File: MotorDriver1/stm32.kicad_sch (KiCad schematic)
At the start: 1 part, among them IC1 STM32C092RCT6

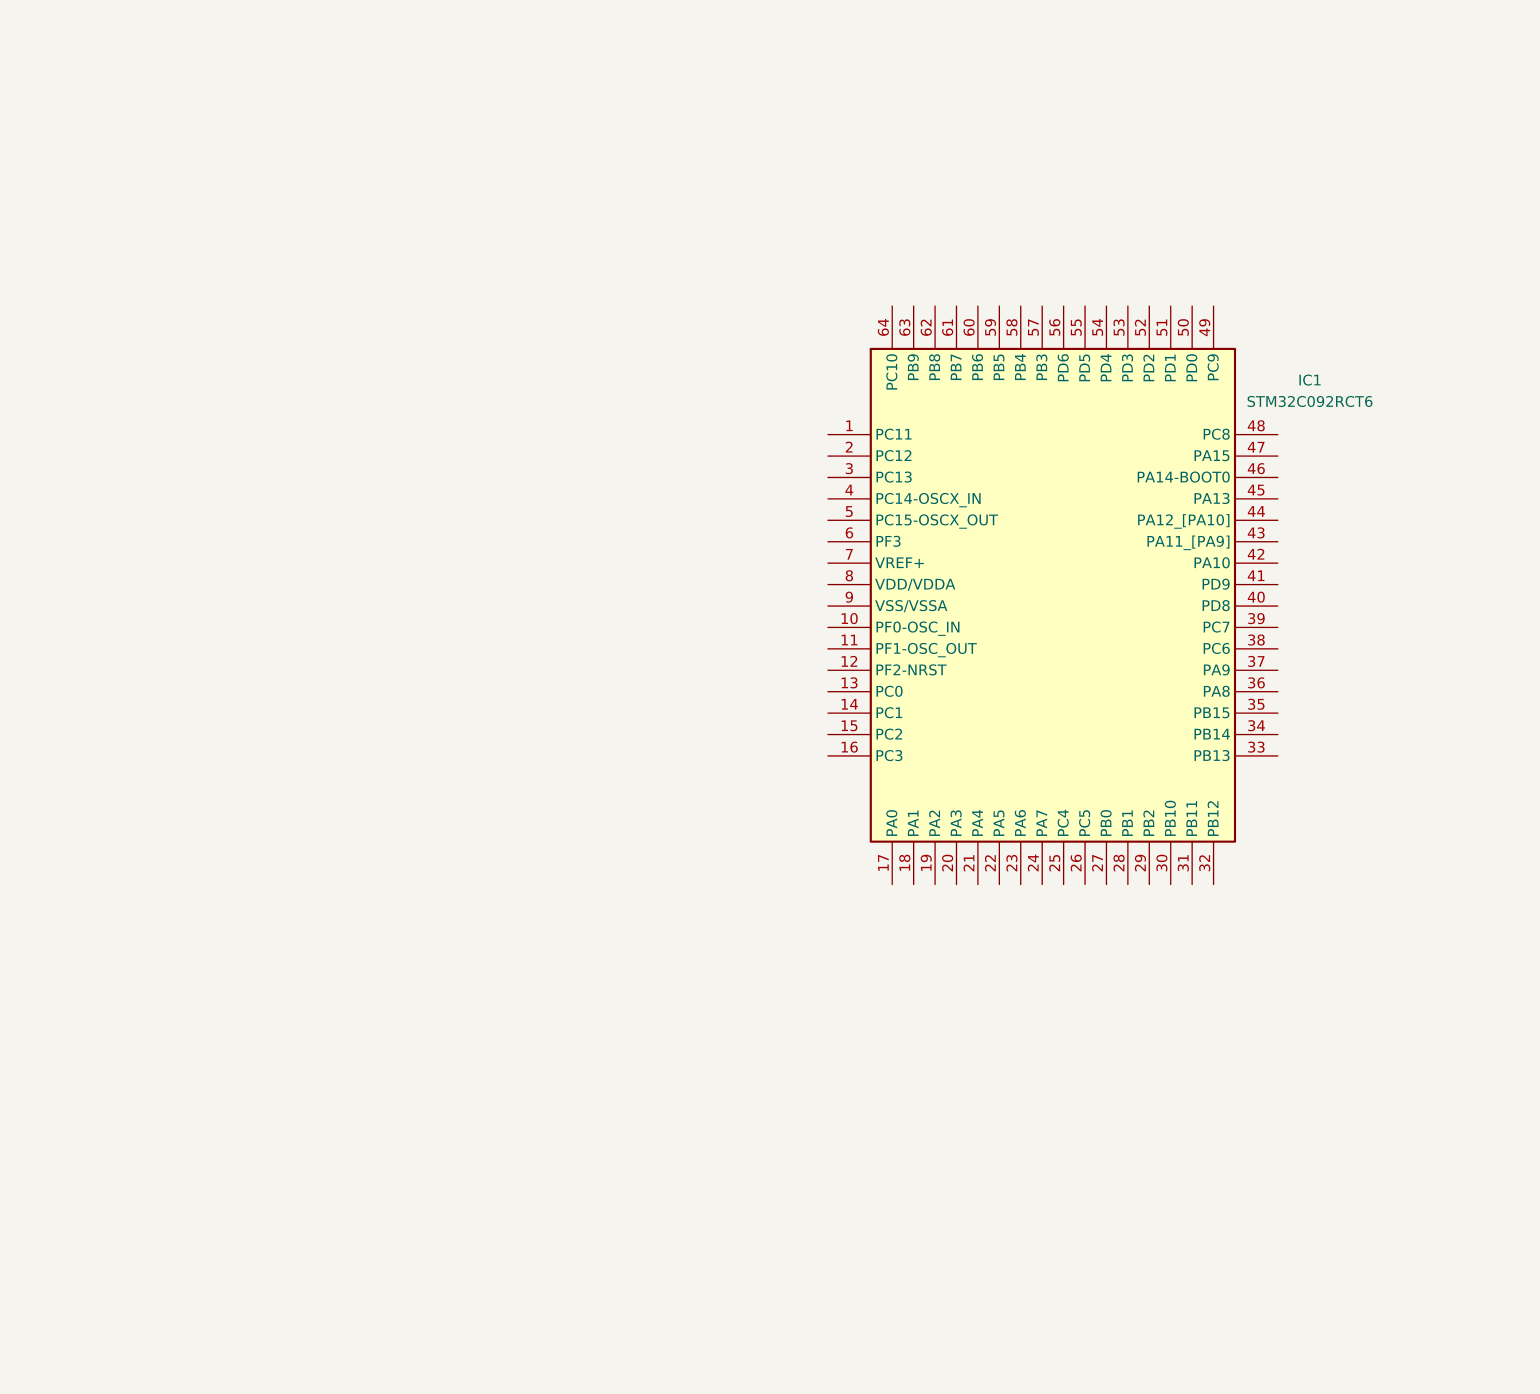
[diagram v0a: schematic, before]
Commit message: Edited STM32 schematic
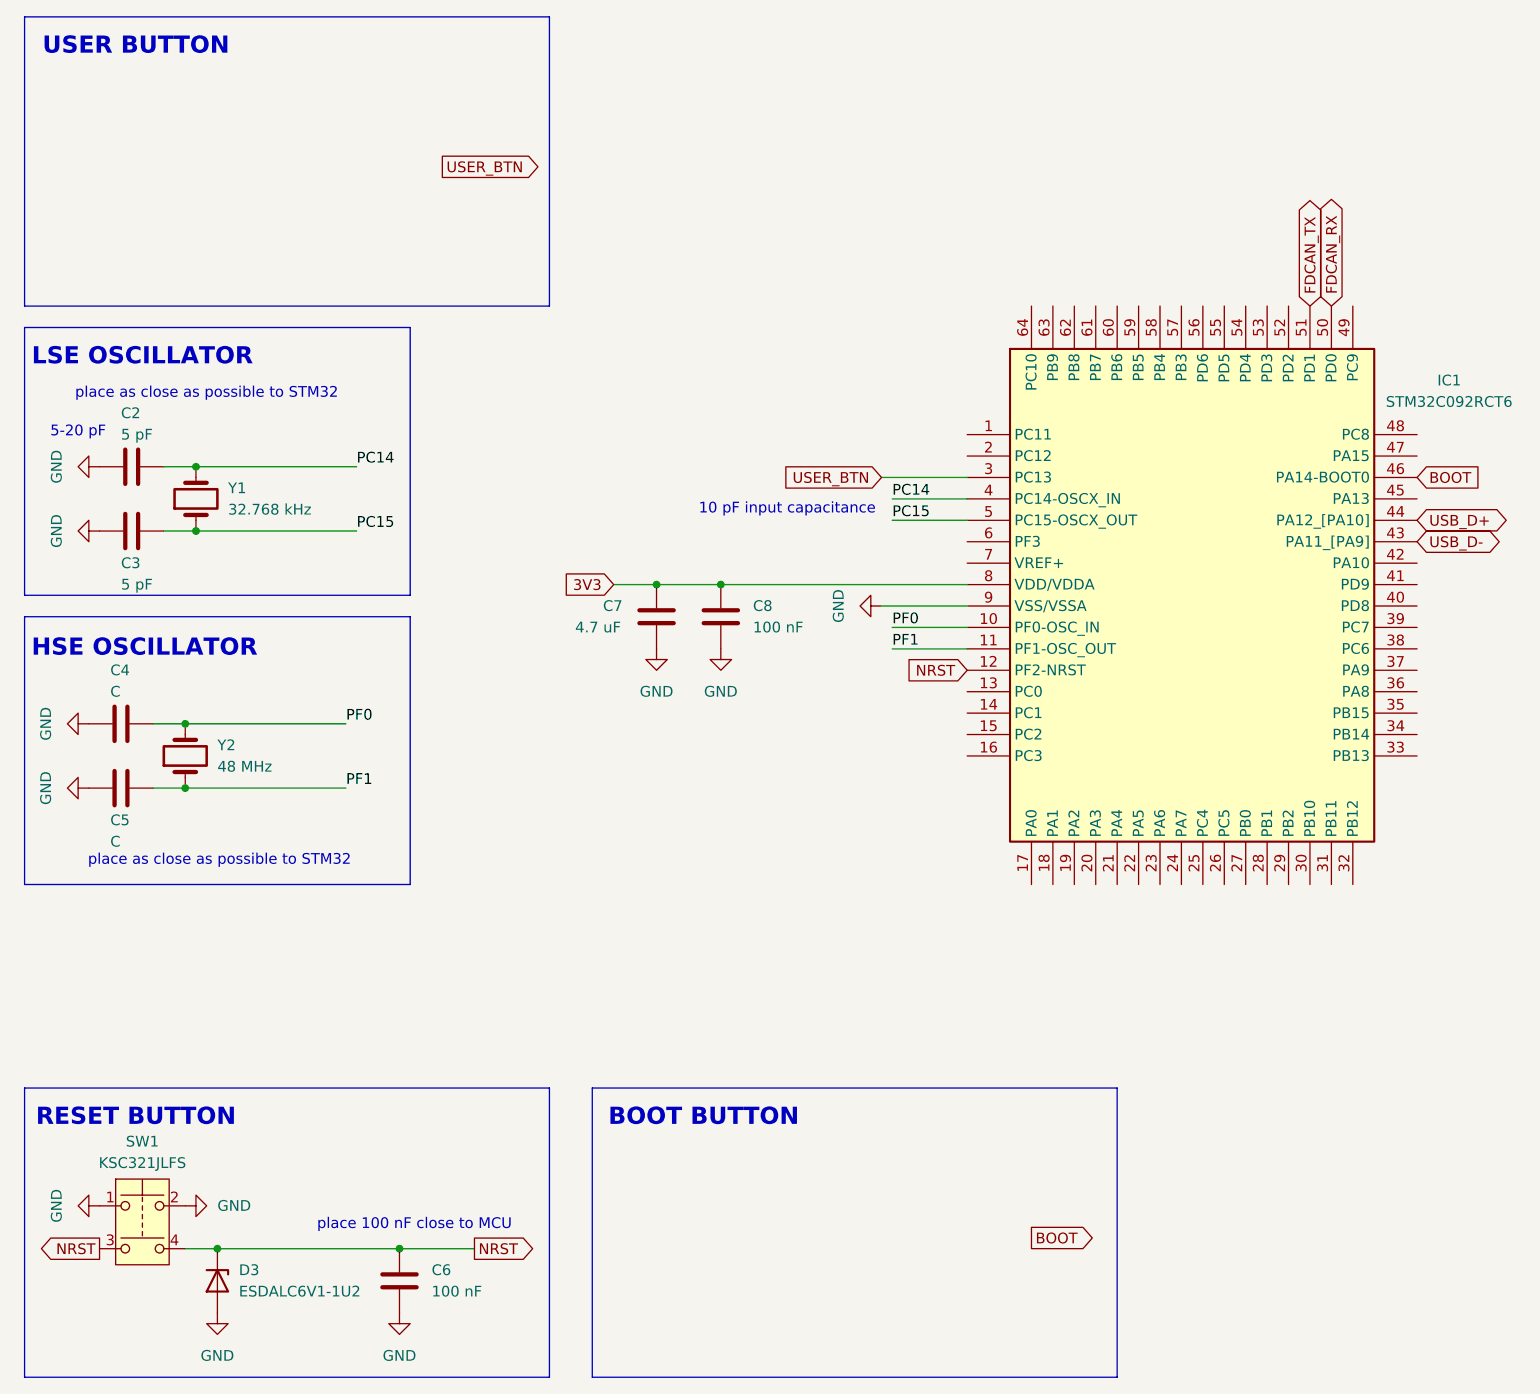
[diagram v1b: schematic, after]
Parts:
- added C2, C3: 5 pF, symbol Device:C
- added C4, C5: C, symbol Device:C
- added C6, C8: 100 nF, symbol Device:C
- added C7: 4.7 uF, symbol Device:C
- added D3: ESDALC6V1-1U2, symbol Device:D_Zener
- added SW1: KSC321JLFS, symbol Switch:SW_Push_Dual
- added Y1: 32.768 kHz, symbol Device:Crystal
- added Y2: 48 MHz, symbol Device:Crystal
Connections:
- net PF0: now reaches IC1.10 (PF0-OSC_IN)
- net PF0: now also C4.2, Y2.2
- net PF1: now reaches IC1.11 (PF1-OSC_OUT)
- net PF1: now also C5.1, Y2.1
- net NRST: now reaches IC1.12 (PF2-NRST)
- net NRST: now also C6.1, D3.1 (K), SW1.3, SW1.4
- net USER_BTN: now reaches IC1.3 (PC13)
- net PC14: now reaches IC1.4 (PC14-OSCX_IN)
- net PC14: now also C2.2, Y1.2
- net USB_D-: now reaches IC1.43 (PA11_[PA9])
- net USB_D+: now reaches IC1.44 (PA12_[PA10])
- net BOOT: now reaches IC1.46 (PA14-BOOT0)
- net PC15: now reaches IC1.5 (PC15-OSCX_OUT)
- net PC15: now also C3.1, Y1.1
- net FDCAN_RX: now reaches IC1.50 (PD0)
- net FDCAN_TX: now reaches IC1.51 (PD1)
- net 3V3: now reaches IC1.8 (VDD/VDDA)
- net 3V3: now also C7.2, C8.1
- net GND: now reaches IC1.9 (VSS/VSSA)
- net GND: now also C2.1, C3.2, C4.1, C5.2, C6.2, C7.1, C8.2, D3.2 (A), SW1.1, SW1.2
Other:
- note added: "10 pF input capacitance"
- note added: "5-20 pF"
- note added: "BOOT BUTTON"
- note added: "HSE OSCILLATOR"
- note added: "LSE OSCILLATOR"
- note added: "RESET BUTTON"
- note added: "USER BUTTON"
- note added: "place 100 nF close to MCU"
- note added: "place as close as possible to STM32"
- moved on the sheet: IC1

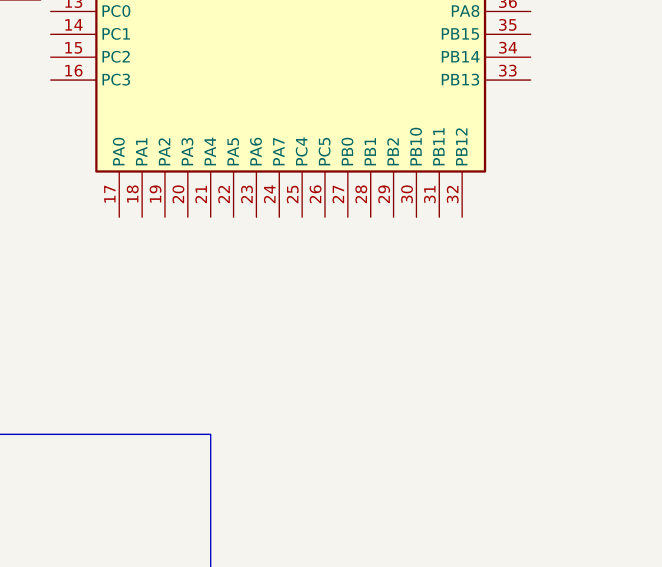
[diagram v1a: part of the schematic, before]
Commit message: Added net labels and global lables to motor driver
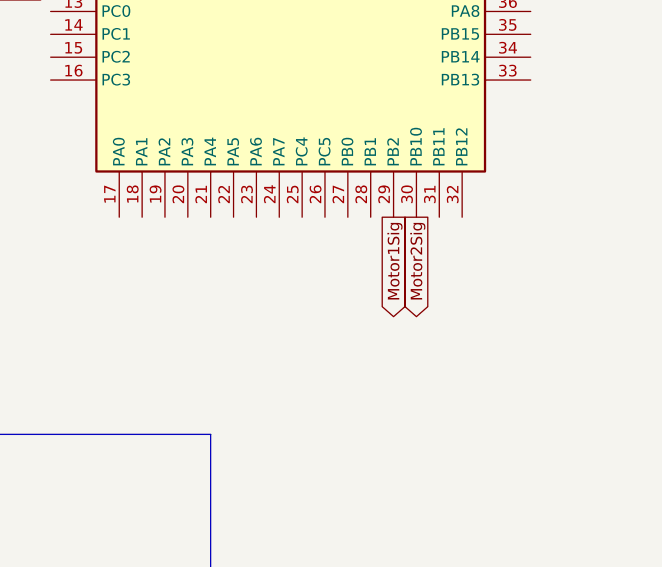
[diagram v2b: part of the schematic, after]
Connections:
- net Motor1Sig: now reaches IC1.29 (PB2)
- net Motor2Sig: now reaches IC1.30 (PB10)
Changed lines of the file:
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@@
+		)
+	)
+	(global_label "Motor1Sig"
+		(shape output)
+		(at 165.1 133.35 270)
+		(fields_autoplaced yes)
+		(effects
+			(font
+				(size 1.27 1.27)
+			)
+			(justify right)
+		)
+		(property "Intersheetrefs" "${INTERSHEET_REFS}"
+			(at 165.1 145.7693 90)
+			(effects
+				(font
+					(size 1.27 1.27)
+				)
+				(justify right)
+				(hide yes)
+			)
 		)
 	)
@@
 		)
 	)
+	(global_label "Motor2Sig"
+		(shape output)
+		(at 167.64 133.35 270)
+		(fields_autoplaced yes)
+		(effects
+			(font
+				(size 1.27 1.27)
+			)
+			(justify right)
+		)
+		(property "Intersheetrefs" "${INTERSHEET_REFS}"
+			(at 167.64 145.7693 90)
+			(effects
+				(font
+					(size 1.27 1.27)
+				)
+				(justify right)
+				(hide yes)
+			)
+		)
+	)
 	(global_label "BOOT"
 		(shape output)
@@
 		(dnp no)
 		(fields_autoplaced yes)
-		(property "Reference" "D3"
+		(property "Reference" "D?"
 			(at 40.64 179.0699 90)
 			(effects
@@
 				)
 			)
+			(project "stm32"
+				(path "/85f32bc1-9169-480e-a658-3b951d4944e0"
+					(reference "D?")
+					(unit 1)
+				)
+			)
 		)
 	)
@@
 		(dnp no)
 		(fields_autoplaced yes)
-		(property "Reference" "C6"
+		(property "Reference" "C?"
 			(at 63.5 179.0699 0)
 			(effects
@@
 				)
 			)
+			(project "stm32"
+				(path "/85f32bc1-9169-480e-a658-3b951d4944e0"
+					(reference "C?")
+					(unit 1)
+				)
+			)
 		)
 	)
@@
 		(dnp no)
 		(fields_autoplaced yes)
-		(property "Reference" "SW1"
+		(property "Reference" "SW?"
 			(at 29.21 163.83 0)
 			(effects
@@
 				)
 			)
+			(project "stm32"
+				(path "/85f32bc1-9169-480e-a658-3b951d4944e0"
+					(reference "SW?")
+					(unit 1)
+				)
+			)
 		)
 	)
@@
 		(on_board yes)
 		(dnp no)
-		(property "Reference" "C7"
+		(property "Reference" "C?"
 			(at 83.82 100.3299 0)
 			(effects
@@
 				)
 			)
+			(project "stm32"
+				(path "/85f32bc1-9169-480e-a658-3b951d4944e0"
+					(reference "C?")
+					(unit 1)
+				)
+			)
 		)
 	)
@@
 		(on_board yes)
 		(dnp no)
-		(property "Reference" "C3"
+		(property "Reference" "C?"
 			(at 26.67 95.2499 90)
 			(effects
@@
 				)
 			)
+			(project "stm32"
+				(path "/85f32bc1-9169-480e-a658-3b951d4944e0"
+					(reference "C?")
+					(unit 1)
+				)
+			)
 		)
 	)
@@
 		(on_board yes)
 		(dnp no)
-		(property "Reference" "C5"
+		(property "Reference" "C?"
 			(at 25.4 125.7299 90)
 			(effects
@@
 				)
 			)
+			(project "stm32"
+				(path "/85f32bc1-9169-480e-a658-3b951d4944e0"
+					(reference "C?")
+					(unit 1)
+				)
+			)
 		)
 	)
@@
 		(dnp no)
 		(fields_autoplaced yes)
-		(property "Reference" "#PWR012"
+		(property "Reference" "#PWR?"
 			(at 38.1 190.5 0)
 			(effects
@@
 				)
 			)
+			(project "stm32"
+				(path "/85f32bc1-9169-480e-a658-3b951d4944e0"
+					(reference "#PWR?")
+					(unit 1)
+				)
+			)
 		)
 	)
@@
 		(on_board yes)
 		(dnp no)
-		(property "Reference" "C8"
+		(property "Reference" "C?"
 			(at 101.6 100.3299 0)
 			(effects
@@
 				)
 			)
+			(project "stm32"
+				(path "/85f32bc1-9169-480e-a658-3b951d4944e0"
+					(reference "C?")
+					(unit 1)
+				)
+			)
 		)
 	)
@@
 		(dnp no)
 		(fields_autoplaced yes)
-		(property "Reference" "#PWR013"
+		(property "Reference" "#PWR?"
 			(at 17.78 171.45 0)
 			(effects
@@
 				)
 			)
+			(project "stm32"
+				(path "/85f32bc1-9169-480e-a658-3b951d4944e0"
+					(reference "#PWR?")
+					(unit 1)
+				)
+			)
 		)
 	)
@@
 		(on_board yes)
 		(dnp no)
-		(property "Reference" "C2"
+		(property "Reference" "C?"
 			(at 26.67 77.4699 90)
 			(effects
@@
 				)
 			)
+			(project "stm32"
+				(path "/85f32bc1-9169-480e-a658-3b951d4944e0"
+					(reference "C?")
+					(unit 1)
+				)
+			)
 		)
 	)
@@
 		(dnp no)
 		(fields_autoplaced yes)
-		(property "Reference" "#PWR010"
+		(property "Reference" "#PWR?"
 			(at 16.51 121.92 0)
 			(effects
@@
 				)
 			)
+			(project "stm32"
+				(path "/85f32bc1-9169-480e-a658-3b951d4944e0"
+					(reference "#PWR?")
+					(unit 1)
+				)
+			)
 		)
 	)
@@
 		(dnp no)
 		(fields_autoplaced yes)
-		(property "Reference" "#PWR09"
+		(property "Reference" "#PWR?"
 			(at 16.51 114.3 0)
 			(effects
@@
 				)
 			)
+			(project "stm32"
+				(path "/85f32bc1-9169-480e-a658-3b951d4944e0"
+					(reference "#PWR?")
+					(unit 1)
+				)
+			)
 		)
 	)
@@
 		(on_board yes)
 		(dnp no)
-		(property "Reference" "C4"
+		(property "Reference" "C?"
 			(at 25.4 107.9499 90)
 			(effects
@@
 				)
 			)
+			(project "stm32"
+				(path "/85f32bc1-9169-480e-a658-3b951d4944e0"
+					(reference "C?")
+					(unit 1)
+				)
+			)
 		)
 	)
@@
 		(dnp no)
 		(fields_autoplaced yes)
-		(property "Reference" "IC1"
+		(property "Reference" "IC?"
 			(at 184.15 73.5898 0)
 			(effects
@@
 				)
 			)
+			(project "stm32"
+				(path "/85f32bc1-9169-480e-a658-3b951d4944e0"
+					(reference "IC?")
+					(unit 1)
+				)
+			)
 		)
 	)
@@
 		(dnp no)
 		(fields_autoplaced yes)
-		(property "Reference" "Y2"
+		(property "Reference" "Y?"
 			(at 38.1 116.8399 90)
 			(effects
@@
 				)
 			)
+			(project "stm32"
+				(path "/85f32bc1-9169-480e-a658-3b951d4944e0"
+					(reference "Y?")
+					(unit 1)
+				)
+			)
 		)
 	)
@@
 		(dnp no)
 		(fields_autoplaced yes)
-		(property "Reference" "Y1"
+		(property "Reference" "Y?"
 			(at 39.37 86.3599 90)
 			(effects
@@
 				)
 			)
+			(project "stm32"
+				(path "/85f32bc1-9169-480e-a658-3b951d4944e0"
+					(reference "Y?")
+					(unit 1)
+				)
+			)
 		)
 	)
@@
 		(dnp no)
 		(fields_autoplaced yes)
-		(property "Reference" "#PWR015"
+		(property "Reference" "#PWR?"
 			(at 90.17 111.76 0)
 			(effects
@@
 				)
 			)
+			(project "stm32"
+				(path "/85f32bc1-9169-480e-a658-3b951d4944e0"
+					(reference "#PWR?")
+					(unit 1)
+				)
+			)
 		)
 	)
@@
 		(dnp no)
 		(fields_autoplaced yes)
-		(property "Reference" "#PWR08"
+		(property "Reference" "#PWR?"
 			(at 110.49 100.33 0)
 			(effects
@@
 				)
 			)
+			(project "stm32"
+				(path "/85f32bc1-9169-480e-a658-3b951d4944e0"
+					(reference "#PWR?")
+					(unit 1)
+				)
+			)
 		)
 	)
@@
 		(dnp no)
 		(fields_autoplaced yes)
-		(property "Reference" "#PWR014"
+		(property "Reference" "#PWR?"
 			(at 40.64 171.45 0)
 			(effects
@@
 				)
 			)
+			(project "stm32"
+				(path "/85f32bc1-9169-480e-a658-3b951d4944e0"
+					(reference "#PWR?")
+					(unit 1)
+				)
+			)
 		)
 	)
@@
 		(dnp no)
 		(fields_autoplaced yes)
-		(property "Reference" "#PWR016"
+		(property "Reference" "#PWR?"
 			(at 97.79 111.76 0)
 			(effects
@@
 				)
 			)
+			(project "stm32"
+				(path "/85f32bc1-9169-480e-a658-3b951d4944e0"
+					(reference "#PWR?")
+					(unit 1)
+				)
+			)
 		)
 	)
@@
 		(dnp no)
 		(fields_autoplaced yes)
-		(property "Reference" "#PWR07"
+		(property "Reference" "#PWR?"
 			(at 17.78 83.82 0)
 			(effects
@@
 				)
 			)
+			(project "stm32"
+				(path "/85f32bc1-9169-480e-a658-3b951d4944e0"
+					(reference "#PWR?")
+					(unit 1)
+				)
+			)
 		)
 	)
@@
 		(dnp no)
 		(fields_autoplaced yes)
-		(property "Reference" "#PWR011"
+		(property "Reference" "#PWR?"
 			(at 59.69 190.5 0)
 			(effects
@@
 				)
 			)
+			(project "stm32"
+				(path "/85f32bc1-9169-480e-a658-3b951d4944e0"
+					(reference "#PWR?")
+					(unit 1)
+				)
+			)
 		)
 	)
@@
 		(dnp no)
 		(fields_autoplaced yes)
-		(property "Reference" "#PWR05"
+		(property "Reference" "#PWR?"
 			(at 17.78 91.44 0)
 			(effects
@@
 				)
 			)
-		)
-	)
+			(project "stm32"
+				(path "/85f32bc1-9169-480e-a658-3b951d4944e0"
+					(reference "#PWR?")
+					(unit 1)
+				)
+			)
+		)
+	)
+	(sheet_instances
+		(path "/"
+			(page "1")
+		)
+	)
+	(embedded_fonts no)
 )

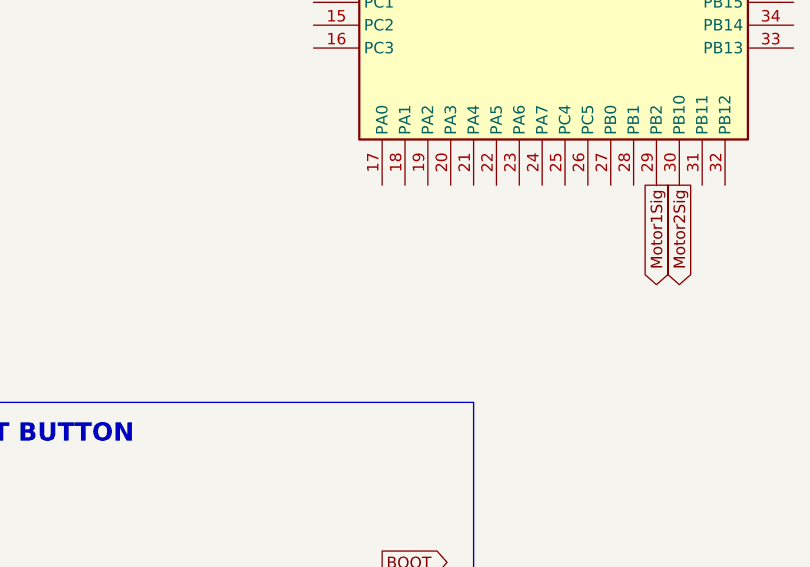
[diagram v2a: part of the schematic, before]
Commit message: added pressure sensor and flags to STM need op amp rails
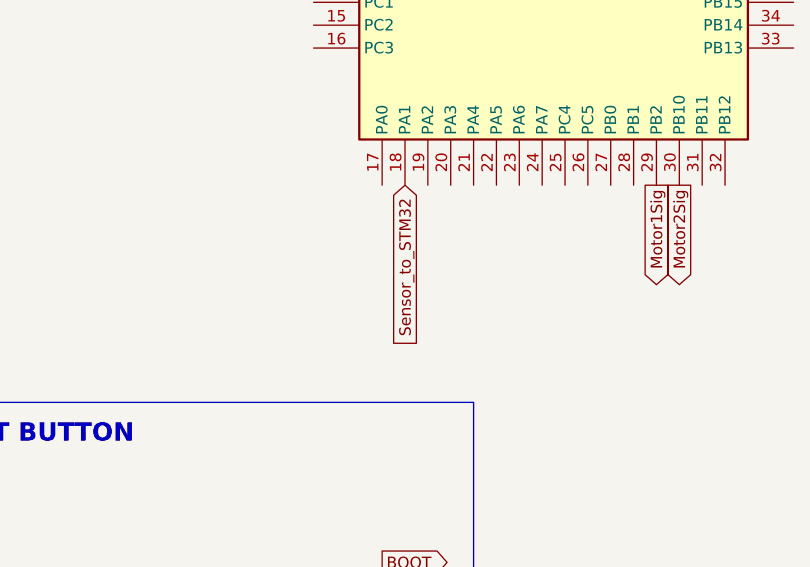
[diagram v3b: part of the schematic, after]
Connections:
- net Sensor_to_STM32: now reaches IC1.18 (PA1)
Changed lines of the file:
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@@
+		)
+	)
+	(global_label "Sensor_to_STM32"
+		(shape input)
+		(at 137.16 133.35 270)
+		(fields_autoplaced yes)
+		(effects
+			(font
+				(size 1.27 1.27)
+			)
+			(justify right)
+		)
+		(property "Intersheetrefs" "${INTERSHEET_REFS}"
+			(at 137.16 152.603 90)
+			(effects
+				(font
+					(size 1.27 1.27)
+				)
+				(justify right)
+				(hide yes)
+			)
 		)
 	)
